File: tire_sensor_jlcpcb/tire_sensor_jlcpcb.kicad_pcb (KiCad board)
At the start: 4 copper layers, 33 x 26 mm, 37 parts, among them J1 Conn_02x05_Odd_Even, U2 DPS368, U3 LSM6DS3, X1 NX2016SA-32MHZ-EXS00A-CS06654, X2 32.768kHz

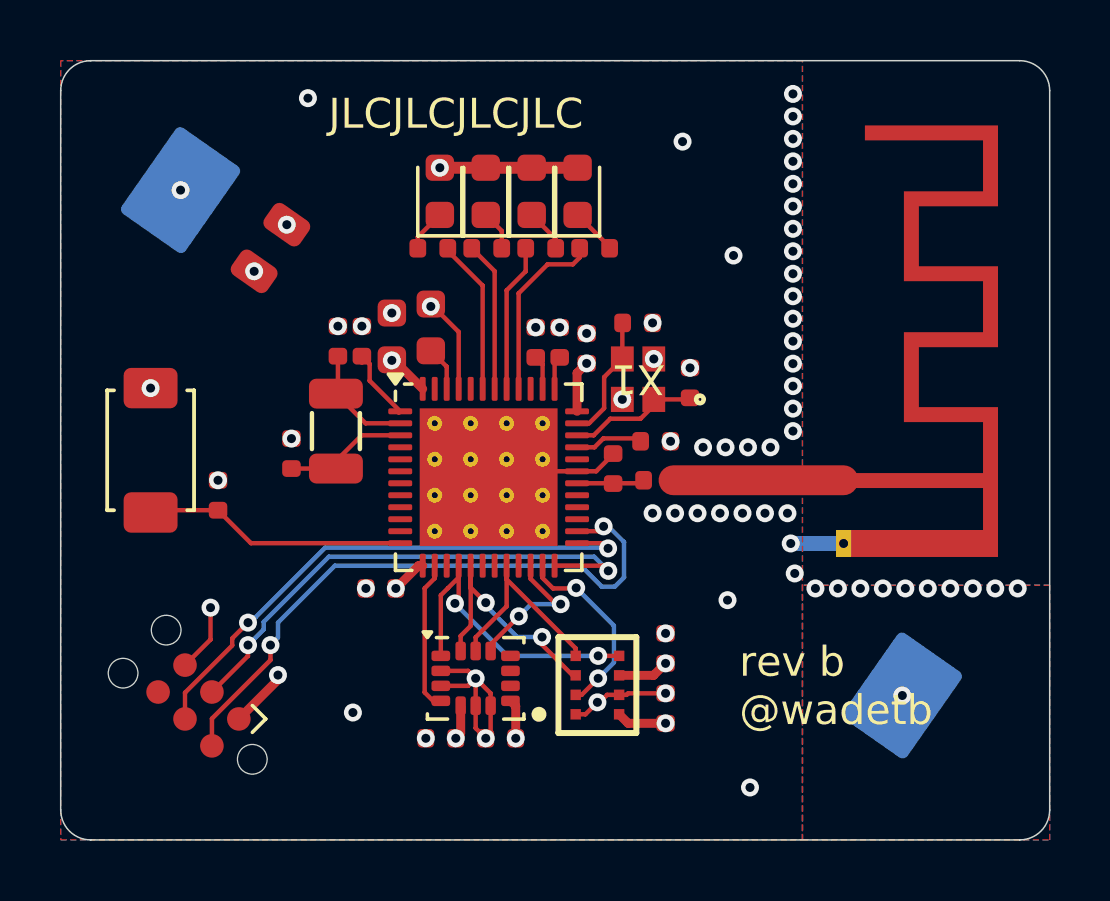
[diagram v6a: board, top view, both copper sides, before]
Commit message: RF antenna tweaks
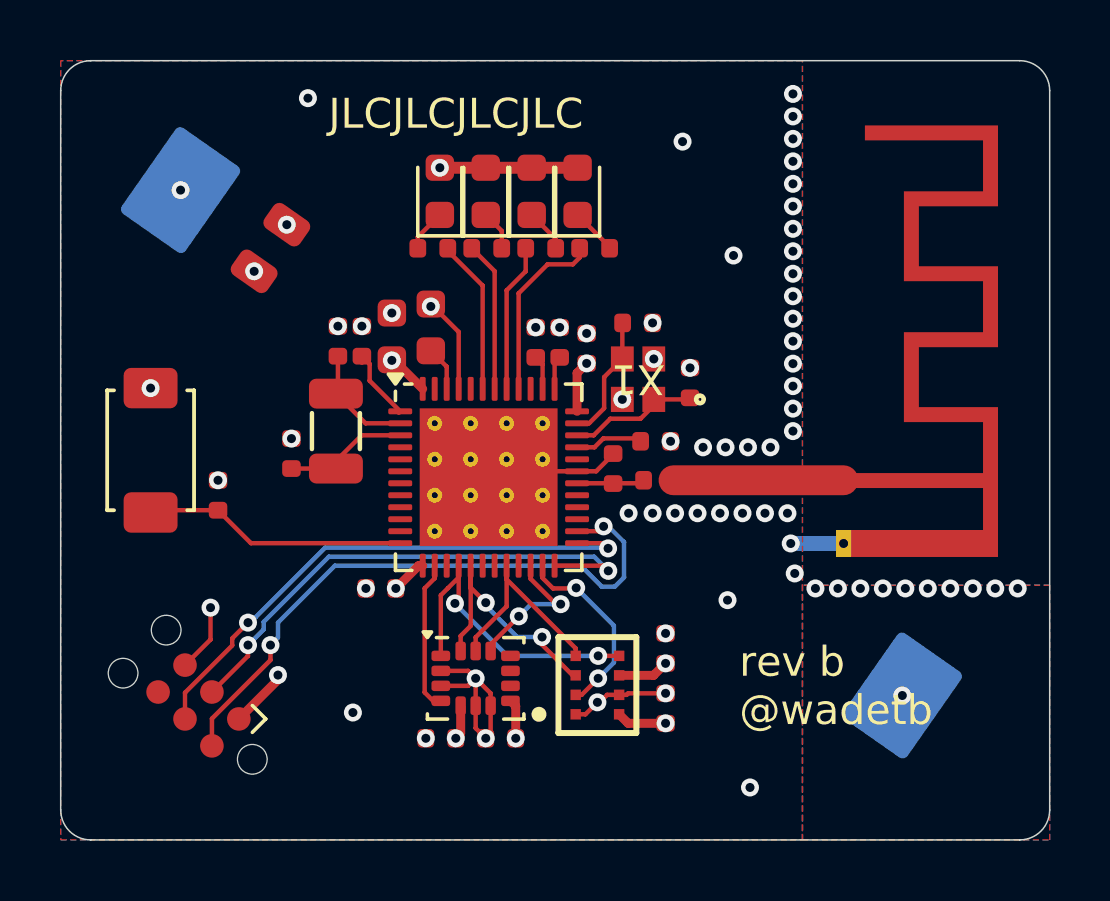
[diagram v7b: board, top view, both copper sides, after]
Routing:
- net GND: vias 69 -> 70
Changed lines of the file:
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@@
+	)
+	(via
+		(at 174.76656 106.990685)
+		(size 0.6)
+		(drill 0.3)
+		(layers "F.Cu" "B.Cu")
+		(free yes)
+		(net 3)
 	)
 	(via
@@
 		(net 0)
 		(net_name "")
-		(layers "In1.Cu" "In2.Cu")
+		(layers "F.Cu" "In1.Cu" "In2.Cu")
 		(hatch edge 0.5)
 		(connect_pads
